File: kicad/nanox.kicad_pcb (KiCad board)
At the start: 4 copper layers, 61.7 x 15.9 mm, 139 parts, among them P1 likely an ESD protection diod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, P2 likely an ESD protection diod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, P3 likely an ESD protection diod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, P4 likely an ESD protection diod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, P5 likely an ESD protection diod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, SW1 push button, left, SW2 push button, right, X1 ?, X10 TI TLV61046A boost converter 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, X11 unknown, marked AF, likely a 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, X12 unknown, likely a P-channel M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, X2 likely an N-channel MOSFET: t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, X3 likely an N-channel MOSFET: t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, X4 ?, X5 ?, X6 ?, X7 ?, X8 ?, X9 NXP PMBZ5246B 16 V Zener diod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, Y1 crystal, likely the 32 MHz HSE

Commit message: Identify PWR2 as an ST STC3115AIQT battery fuel gauge
Its marking reads O205, ST's code for the STC3115AIQT (DFN10, 2 x 3 mm,
for 4.2 V cells), and its pinout matches every traced pin: ALM to MCU
PA10, SDA/SCL on I2C1, CG on pack - to sense the current across X4,
BATD/CD through R12, VCC on battery +, VIN through the R13/C6 filter.
Pin 5 is GND, now joined to the ground pour. X4 is confirmed as the
current-sense resistor.

Co-Authored-By: Claude Opus 5.5 <noreply@anthropic.com>
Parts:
- PWR2: value unknown -> ST STC3115AIQT battery fuel gauge
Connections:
- net Net-T48 renamed Fuel gauge BATD
- net Net-T62 renamed Fuel gauge ALM
- net Net-T65 renamed Fuel gauge VIN
- PWR2 pad 5: (no net) -> GND

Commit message: Ground the fuel gauge's RSTIO pin (7) as well as GND (5)
Co-Authored-By: Claude Opus 5.5 <noreply@anthropic.com>
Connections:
- PWR2 pad 7: (no net) -> GND
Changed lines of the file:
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@@
+	(footprint ""
+		(layer "F.Cu")
+		(at 20.41369 14.130952)
+		(descr "DFN10, 2 x 3 mm; Gas gauge for the Li-ion battery (the A version, for 4.2 V cells), read by the MCU over I2C1. Marked O205, ST's code for the STC3115AIQT (8128 is likely a date or lot code). Its pinout matches every traced pin with pin 1 at the first corner outlined: ALM (1) to MCU PA10, SDA (2), SCL (3), GND (5) and RSTIO (7) through the ground pour, CG (6) on pack - to sense the current across X4, BATD/CD (8) through R12, VCC (9) on battery +, VIN (10) on battery + through the R13/C6 filter; NC (4) unconnected")
+		(property "Reference" "PWR2"
+			(at 0 0 0)
+			(layer "F.SilkS")
+			(effects
+				(font
+					(size 0.5 0.5)
+					(thickness 0.08)
+				)
+			)
+		)
+		(property "Value" "ST STC3115AIQT battery fuel gauge"
+			(at 0 0 0)
+			(layer "F.Fab")
+			(hide yes)
+			(effects
+				(font
+					(size 1.27 1.27)
+				)
+			)
+		)
+		(property "Datasheet" ""
+			(at 0 0 0)
+			(layer "F.Fab")
+			(hide yes)
+			(effects
+				(font
+					(size 1.27 1.27)
+				)
+			)
+		)
+		(property "Description" ""
+			(at 0 0 0)
+			(layer "F.Fab")
+			(hide yes)
+			(effects
+				(font
+					(size 1.27 1.27)
+				)
+			)
+		)
+		(duplicate_pad_numbers_are_jumpers no)
+		(fp_line
+			(start -1.485119 -0.952381)
+			(end -1.425595 0.916667)
+			(stroke
+				(width 0.08)
+				(type default)
+			)
+			(layer "F.Fab")
+		)
+		(fp_line
+			(start -1.425595 0.916667)
+			(end 1.479167 0.940476)
+			(stroke
+				(width 0.08)
+				(type default)
+			)
+			(layer "F.Fab")
+		)
+		(fp_line
+			(start 1.431548 -0.904762)
+			(end -1.485119 -0.952381)
+			(stroke
+				(width 0.08)
+				(type default)
+			)
+			(layer "F.Fab")
+		)
+		(fp_line
+			(start 1.479167 0.940476)
+			(end 1.431548 -0.904762)
+			(stroke
+				(width 0.08)
+				(type default)
+			)
+			(layer "F.Fab")
+		)
+		(pad "1" smd rect
+			(at 0.979167 -0.916667 269.0646418)
+			(size 0.6 0.25)
+			(layers "F.Cu" "F.Mask" "F.Paste")
+			(net "Fuel gauge ALM")
+			(thermal_bridge_angle 45)
+		)
+		(pad "2" smd rect
+			(at 0.479167 -0.916667 269.0646418)
+			(size 0.6 0.25)
+			(layers "F.Cu" "F.Mask" "F.Paste")
+			(net "I2C1 SDA")
+			(thermal_bridge_angle 45)
+		)
+		(pad "3" smd rect
+			(at -0.032738 -0.928572 269.0646418)
+			(size 0.6 0.25)
+			(layers "F.Cu" "F.Mask" "F.Paste")
+			(net "I2C1 SCL")
+			(thermal_bridge_angle 45)
+		)
+		(pad "4" smd rect
+			(at -0.532738 -0.940476 269.0646418)
+			(size 0.6 0.25)
+			(layers "F.Cu" "F.Mask" "F.Paste")
+			(thermal_bridge_angle 45)
+		)
+		(pad "5" smd rect
+			(at -1.032738 -0.940476 269.0646418)
+			(size 0.6 0.25)
+			(layers "F.Cu" "F.Mask" "F.Paste")
+			(net "GND")
+			(thermal_bridge_angle 45)
+		)
+		(pad "6" smd rect
+			(at -0.973214 0.916667 269.0646418)
+			(size 0.6 0.25)
+			(layers "F.Cu" "F.Mask" "F.Paste")
+			(net "Pack -?")
+			(thermal_bridge_angle 45)
+		)
+		(pad "7" smd rect
+			(at -0.473214 0.928571 269.0646418)
+			(size 0.6 0.25)
+			(layers "F.Cu" "F.Mask" "F.Paste")
+			(net "GND")
+			(thermal_bridge_angle 45)
+		)
+		(pad "8" smd rect
+			(at 0.026786 0.928571 269.0646418)
+			(size 0.6 0.25)
+			(layers "F.Cu" "F.Mask" "F.Paste")
+			(net "Fuel gauge BATD")
+			(thermal_bridge_angle 45)
+		)
+		(pad "9" smd rect
+			(at 0.526786 0.928571 269.0646418)
+			(size 0.6 0.25)
+			(layers "F.Cu" "F.Mask" "F.Paste")
+			(net "Battery +")
+			(thermal_bridge_angle 45)
+		)
+		(pad "10" smd rect
+			(at 1.026786 0.940476 269.0646418)
+			(size 0.6 0.25)
+			(layers "F.Cu" "F.Mask" "F.Paste")
+			(net "Fuel gauge VIN")
+			(thermal_bridge_angle 45)
+		)
+		(embedded_fonts no)
+		(model "/home/magicaltux/projects/ledger_nano_x_pads/kicad/3d/PWR2.wrl"
+			(offset
+				(xyz 0 0 0)
+			)
+			(scale
+				(xyz 1 1 1)
+			)
+			(rotate
+				(xyz 0 0 0)
+			)
+		)
+	)
 	(footprint ""
 		(layer "F.Cu")
@@
 			(offset
 				(xyz 0 0 0)
-			)
-			(scale
-				(xyz 1 1 1)
-			)
-			(rotate
-				(xyz 0 0 0)
-			)
-		)
-	)
-	(footprint ""
-		(layer "F.Cu")
-		(at 20.41369 14.130952)
-		(descr "DFN10, 2 x 3 mm; Gas gauge for the Li-ion battery (the A version, for 4.2 V cells), read by the MCU over I2C1. Marked O205, ST's code for the STC3115AIQT (8128 is likely a date or lot code). Its pinout matches every traced pin with pin 1 at the first corner outlined: ALM (1) to MCU PA10, SDA (2), SCL (3), GND (5) through the ground pour, CG (6) on pack - to sense the current across X4, BATD/CD (8) through R12, VCC (9) on battery +, VIN (10) on battery + through the R13/C6 filter; NC (4) and RSTIO (7) unconnected")
-		(property "Reference" "PWR2"
-			(at 0 0 0)
-			(layer "F.SilkS")
-			(effects
-				(font
-					(size 0.5 0.5)
-					(thickness 0.08)
-				)
-			)
-		)
-		(property "Value" "ST STC3115AIQT battery fuel gauge"
-			(at 0 0 0)
-			(layer "F.Fab")
-			(hide yes)
-			(effects
-				(font
-					(size 1.27 1.27)
-				)
-			)
-		)
-		(property "Datasheet" ""
-			(at 0 0 0)
-			(layer "F.Fab")
-			(hide yes)
-			(effects
-				(font
-					(size 1.27 1.27)
-				)
-			)
-		)
-		(property "Description" ""
-			(at 0 0 0)
-			(layer "F.Fab")
-			(hide yes)
-			(effects
-				(font
-					(size 1.27 1.27)
-				)
-			)
-		)
-		(duplicate_pad_numbers_are_jumpers no)
-		(fp_line
-			(start -1.485119 -0.952381)
-			(end -1.425595 0.916667)
-			(stroke
-				(width 0.08)
-				(type default)
-			)
-			(layer "F.Fab")
-		)
-		(fp_line
-			(start -1.425595 0.916667)
-			(end 1.479167 0.940476)
-			(stroke
-				(width 0.08)
-				(type default)
-			)
-			(layer "F.Fab")
-		)
-		(fp_line
-			(start 1.431548 -0.904762)
-			(end -1.485119 -0.952381)
-			(stroke
-				(width 0.08)
-				(type default)
-			)
-			(layer "F.Fab")
-		)
-		(fp_line
-			(start 1.479167 0.940476)
-			(end 1.431548 -0.904762)
-			(stroke
-				(width 0.08)
-				(type default)
-			)
-			(layer "F.Fab")
-		)
-		(pad "1" smd rect
-			(at 0.979167 -0.916667 269.0646418)
-			(size 0.6 0.25)
-			(layers "F.Cu" "F.Mask" "F.Paste")
-			(net "Fuel gauge ALM")
-			(thermal_bridge_angle 45)
-		)
-		(pad "2" smd rect
-			(at 0.479167 -0.916667 269.0646418)
-			(size 0.6 0.25)
-			(layers "F.Cu" "F.Mask" "F.Paste")
-			(net "I2C1 SDA")
-			(thermal_bridge_angle 45)
-		)
-		(pad "3" smd rect
-			(at -0.032738 -0.928572 269.0646418)
-			(size 0.6 0.25)
-			(layers "F.Cu" "F.Mask" "F.Paste")
-			(net "I2C1 SCL")
-			(thermal_bridge_angle 45)
-		)
-		(pad "4" smd rect
-			(at -0.532738 -0.940476 269.0646418)
-			(size 0.6 0.25)
-			(layers "F.Cu" "F.Mask" "F.Paste")
-			(thermal_bridge_angle 45)
-		)
-		(pad "5" smd rect
-			(at -1.032738 -0.940476 269.0646418)
-			(size 0.6 0.25)
-			(layers "F.Cu" "F.Mask" "F.Paste")
-			(net "GND")
-			(thermal_bridge_angle 45)
-		)
-		(pad "6" smd rect
-			(at -0.973214 0.916667 269.0646418)
-			(size 0.6 0.25)
-			(layers "F.Cu" "F.Mask" "F.Paste")
-			(net "Pack -?")
-			(thermal_bridge_angle 45)
-		)
-		(pad "7" smd rect
-			(at -0.473214 0.928571 269.0646418)
-			(size 0.6 0.25)
-			(layers "F.Cu" "F.Mask" "F.Paste")
-			(thermal_bridge_angle 45)
-		)
-		(pad "8" smd rect
-			(at 0.026786 0.928571 269.0646418)
-			(size 0.6 0.25)
-			(layers "F.Cu" "F.Mask" "F.Paste")
-			(net "Fuel gauge BATD")
-			(thermal_bridge_angle 45)
-		)
-		(pad "9" smd rect
-			(at 0.526786 0.928571 269.0646418)
-			(size 0.6 0.25)
-			(layers "F.Cu" "F.Mask" "F.Paste")
-			(net "Battery +")
-			(thermal_bridge_angle 45)
-		)
-		(pad "10" smd rect
-			(at 1.026786 0.940476 269.0646418)
-			(size 0.6 0.25)
-			(layers "F.Cu" "F.Mask" "F.Paste")
-			(net "Fuel gauge VIN")
-			(thermal_bridge_angle 45)
-		)
-		(embedded_fonts no)
-		(model "/home/magicaltux/projects/ledger_nano_x_pads/kicad/3d/PWR2.wrl"
-			(offset
-				(xyz 0 0 0)

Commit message: Read Y1's marking as 32000 K145 Y: the 32 MHz HSE crystal, confirmed
Co-Authored-By: Claude Opus 5.5 <noreply@anthropic.com>
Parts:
- Y1: value crystal, likely the 32 MHz HSE -> 32 MHz crystal (HSE)
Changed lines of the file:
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@@
-	(footprint ""
-		(layer "F.Cu")
-		(at 34.744047 13.047619)
-		(descr "4 corner pads, ~2.0 x 1.6 mm; Marked 32k0 J 2B; sits where the HSE crystal traces end. Pads are named by corner (top/bottom left/right in the photo) as their numbers are not known; TL and BR go to ground")
-		(property "Reference" "Y1"
-			(at 0 0 0)
-			(layer "F.SilkS")
-			(effects
-				(font
-					(size 0.5 0.5)
-					(thickness 0.08)
-				)
-			)
-		)
-		(property "Value" "crystal, likely the 32 MHz HSE"
-			(at 0 0 0)
-			(layer "F.Fab")
-			(hide yes)
-			(effects
-				(font
-					(size 1.27 1.27)
-				)
-			)
-		)
-		(property "Datasheet" ""
-			(at 0 0 0)
-			(layer "F.Fab")
-			(hide yes)
-			(effects
-				(font
-					(size 1.27 1.27)
-				)
-			)
-		)
-		(property "Description" ""
-			(at 0 0 0)
-			(layer "F.Fab")
-			(hide yes)
-			(effects
-				(font
-					(size 1.27 1.27)
-				)
-			)
-		)
-		(duplicate_pad_numbers_are_jumpers no)
-		(fp_line
-			(start -0.875 -1.02381)
-			(end -0.875 1.023809)
-			(stroke
-				(width 0.08)
-				(type default)
-			)
-			(layer "F.Fab")
-		)
-		(fp_line
-			(start -0.875 1.023809)
-			(end 0.875 1.023809)
-			(stroke
-				(width 0.08)
-				(type default)
-			)
-			(layer "F.Fab")
-		)
-		(fp_line
-			(start 0.875 -1.02381)
-			(end -0.875 -1.02381)
-			(stroke
-				(width 0.08)
-				(type default)
-			)
-			(layer "F.Fab")
-		)
-		(fp_line
-			(start 0.875 1.023809)
-			(end 0.875 -1.02381)
-			(stroke
-				(width 0.08)
-				(type default)
-			)
-			(layer "F.Fab")
-		)
-		(pad "BL" smd rect
-			(at -0.505952 -0.595239)
-			(size 0.738095 0.857142)
-			(layers "F.Cu" "F.Mask" "F.Paste")
-			(net "HSE crystal IN")
-			(thermal_bridge_angle 45)
-		)
-		(pad "BR" smd rect
-			(at 0.505953 -0.595239)
-			(size 0.738095 0.857142)
-			(layers "F.Cu" "F.Mask" "F.Paste")
-			(net "GND")
-			(thermal_bridge_angle 45)
-		)
-		(pad "TL" smd rect
-			(at -0.505952 0.595238)
-			(size 0.738095 0.857142)
-			(layers "F.Cu" "F.Mask" "F.Paste")
-			(net "GND")
-			(thermal_bridge_angle 45)
-		)
-		(pad "TR" smd rect
-			(at 0.505953 0.595238)
-			(size 0.738095 0.857142)
-			(layers "F.Cu" "F.Mask" "F.Paste")
-			(net "HSE crystal OUT")
-			(thermal_bridge_angle 45)
-		)
-		(embedded_fonts no)
-		(model "/home/magicaltux/projects/ledger_nano_x_pads/kicad/3d/Y1.wrl"
-			(offset
-				(xyz 0 0 0)
-			)
-			(scale
-				(xyz 1 1 1)
-			)
-			(rotate
-				(xyz 0 0 0)
-			)
-		)
-	)
 	(footprint ""
 		(layer "F.Cu")
@@
 			)
 		)
+	)
+	(footprint ""
+		(layer "F.Cu")
+		(at 34.744047 13.047619)
+		(descr "4 corner pads, ~2.0 x 1.6 mm; Marked 32000 K145 Y: a 32.000 MHz crystal, the HSE clock the STM32WB needs for its radio; sits where the HSE crystal traces end. Pads are named by corner (top/bottom left/right in the photo) as their numbers are not known; TL and BR go to ground")
+		(property "Reference" "Y1"
+			(at 0 0 0)
+			(layer "F.SilkS")
+			(effects
+				(font
+					(size 0.5 0.5)
+					(thickness 0.08)
+				)
+			)
+		)
+		(property "Value" "32 MHz crystal (HSE)"
+			(at 0 0 0)
+			(layer "F.Fab")
+			(hide yes)
+			(effects
+				(font
+					(size 1.27 1.27)
+				)
+			)
+		)
+		(property "Datasheet" ""
+			(at 0 0 0)
+			(layer "F.Fab")
+			(hide yes)
+			(effects
+				(font
+					(size 1.27 1.27)
+				)
+			)
+		)
+		(property "Description" ""
+			(at 0 0 0)
+			(layer "F.Fab")
+			(hide yes)
+			(effects
+				(font
+					(size 1.27 1.27)
+				)
+			)
+		)
+		(duplicate_pad_numbers_are_jumpers no)
+		(fp_line
+			(start -0.875 -1.02381)
+			(end -0.875 1.023809)
+			(stroke
+				(width 0.08)
+				(type default)
+			)
+			(layer "F.Fab")
+		)
+		(fp_line
+			(start -0.875 1.023809)
+			(end 0.875 1.023809)
+			(stroke
+				(width 0.08)
+				(type default)
+			)
+			(layer "F.Fab")
+		)
+		(fp_line
+			(start 0.875 -1.02381)
+			(end -0.875 -1.02381)
+			(stroke
+				(width 0.08)
+				(type default)
+			)
+			(layer "F.Fab")
+		)
+		(fp_line
+			(start 0.875 1.023809)
+			(end 0.875 -1.02381)
+			(stroke
+				(width 0.08)
+				(type default)
+			)
+			(layer "F.Fab")
+		)
+		(pad "BL" smd rect
+			(at -0.505952 -0.595239)
+			(size 0.738095 0.857142)
+			(layers "F.Cu" "F.Mask" "F.Paste")
+			(net "HSE crystal IN")
+			(thermal_bridge_angle 45)
+		)
+		(pad "BR" smd rect
+			(at 0.505953 -0.595239)
+			(size 0.738095 0.857142)
+			(layers "F.Cu" "F.Mask" "F.Paste")
+			(net "GND")
+			(thermal_bridge_angle 45)
+		)
+		(pad "TL" smd rect
+			(at -0.505952 0.595238)
+			(size 0.738095 0.857142)
+			(layers "F.Cu" "F.Mask" "F.Paste")
+			(net "GND")
+			(thermal_bridge_angle 45)
+		)
+		(pad "TR" smd rect
+			(at 0.505953 0.595238)
+			(size 0.738095 0.857142)
+			(layers "F.Cu" "F.Mask" "F.Paste")
+			(net "HSE crystal OUT")
+			(thermal_bridge_angle 45)
+		)
+		(embedded_fonts no)
+		(model "/home/magicaltux/projects/ledger_nano_x_pads/kicad/3d/Y1.wrl"
+			(offset
+				(xyz 0 0 0)
+			)
+			(scale
+				(xyz 1 1 1)
+			)
+			(rotate
+				(xyz 0 0 0)
+			)
+		)

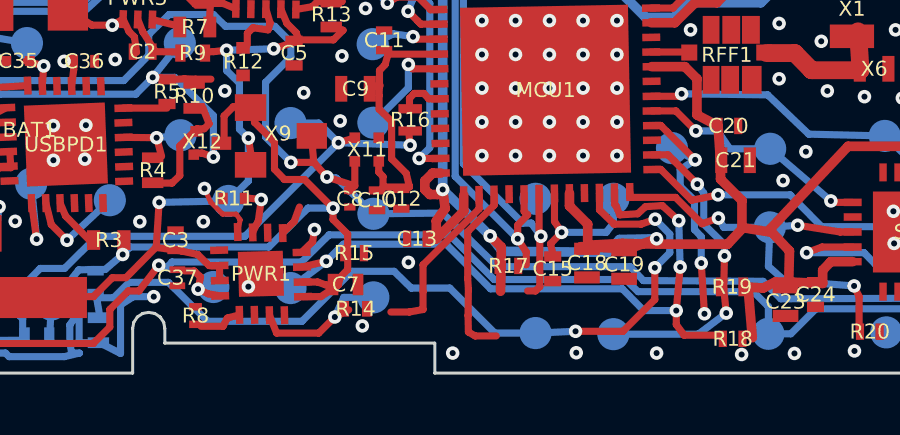
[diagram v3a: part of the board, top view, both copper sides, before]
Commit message: Add the empty LSE crystal footprints as not-populated parts
The MCU's low-speed clock traces end on footprints that are left empty on
the real board: bare, solder-tinned pads for a 32.768 kHz crystal (Y2)
and its two load capacitors (C38, C39). They are now in the model, marked
DNP and excluded from the BOM in KiCad, with no 3D body, so the LSE nets
end on them and the viewers show the bare pads. The MCU must run its RTC
from its internal oscillator instead.

Co-Authored-By: Claude Opus 5.5 <noreply@anthropic.com>
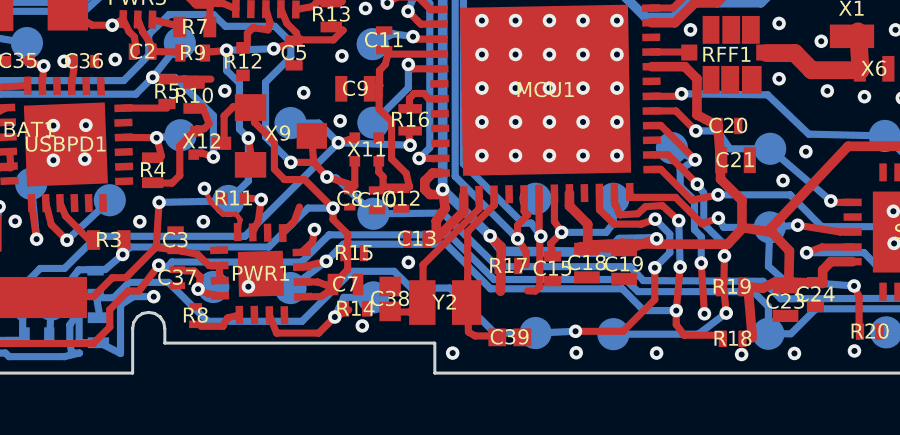
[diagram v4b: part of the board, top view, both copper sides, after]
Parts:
- added C38: not populated: LSE load capacitor, , F.Cu at (24.6, 24.7)
- added C39: not populated: LSE load capacitor, , F.Cu at (28.6, 26.0)
- added Y2: not populated: 32.768 kHz crystal (LSE), , F.Cu at (26.4, 24.8)

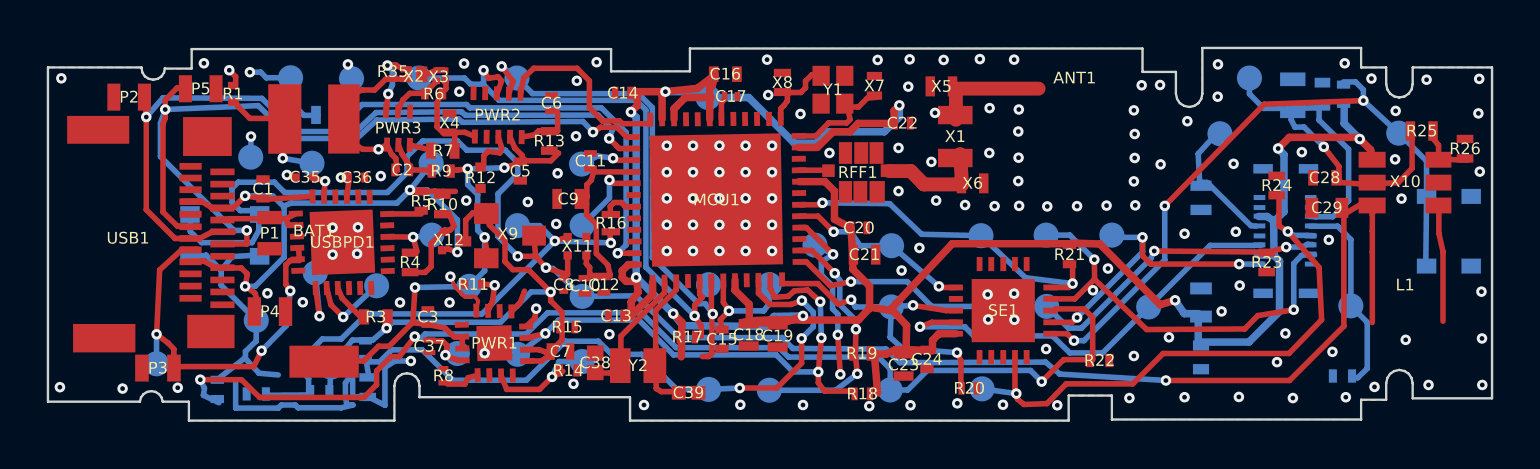
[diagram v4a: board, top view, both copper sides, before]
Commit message: Wire L1 into the OLED boost converter and close the loose resistor and capacitor ends
- L1 gets its two pads: VIN (the pad-19 supply) and the TLV61046A's SW pin
- R24 runs to the +3.3V via below it: a pull-up on OLED SPI CS
- the +3.3V trace by R18 is straightened onto its pad: a pull-up on the
  charger's ST2 status output
- C1, C23, C24, R8 and R28 get their ground ends

Co-Authored-By: Claude Opus 5.5 <noreply@anthropic.com>
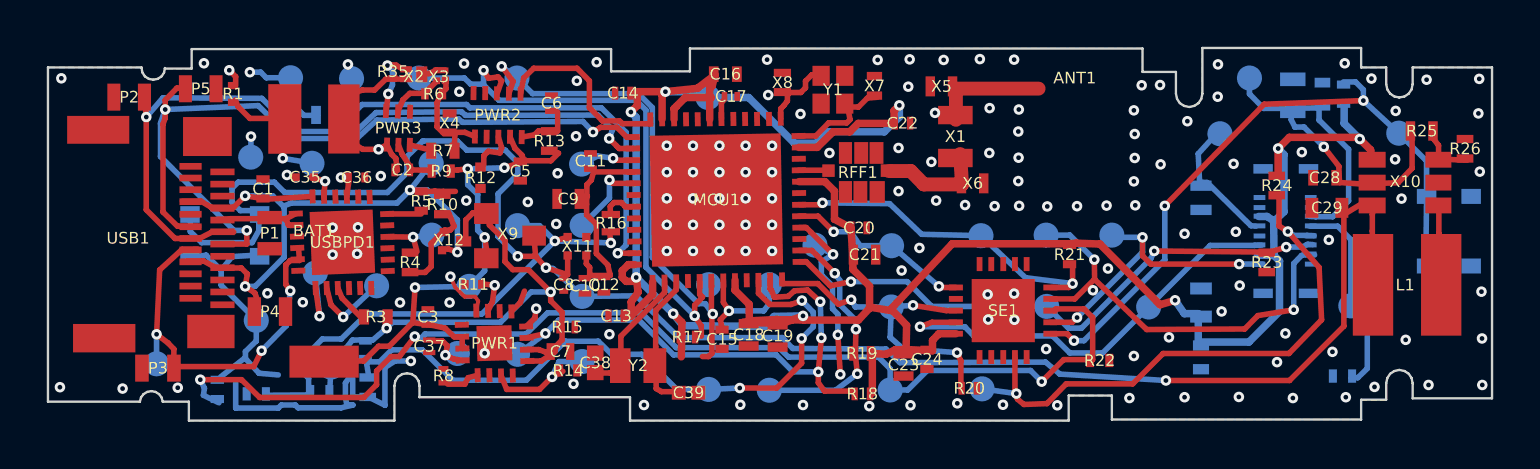
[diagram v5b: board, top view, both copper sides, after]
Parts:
- L1: value unknown, likely a shielded power inductor -> power inductor of the OLED boost converter
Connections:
- C1 pad 2: (no net) -> GND
- C23 pad 1: (no net) -> GND
- C24 pad 1: (no net) -> GND
- R18 pad 2: (no net) -> +3.3V rail
- R24 pad 2: (no net) -> +3.3V rail
- R28 pad 1: (no net) -> GND
- R8 pad 2: (no net) -> GND
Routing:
- net +3.3V rail: track 113.0 -> 114.2 mm
